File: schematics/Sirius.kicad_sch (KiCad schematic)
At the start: 13 parts, among them J1 DE9_Plug, U1 W65C02SxP, U10 MAX232, U2 W65C51NxP, U3 2764, U4 74LS138, U5 74LS138, X1 TFT680, X2 TFT680

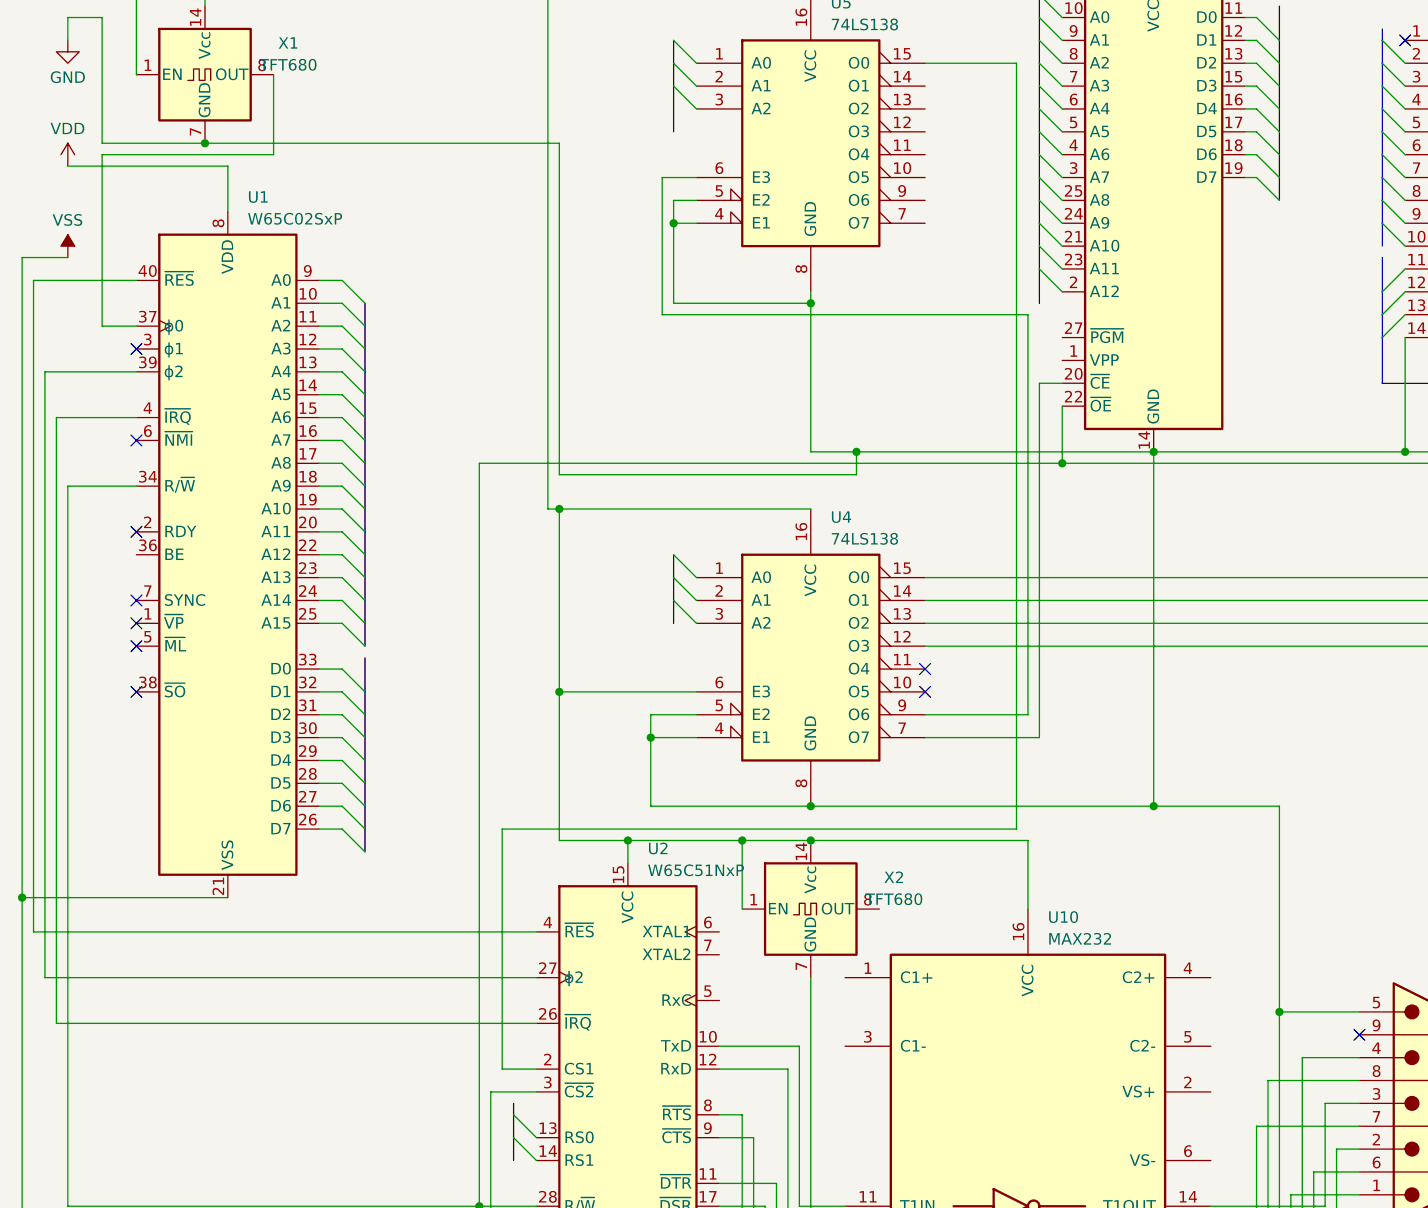
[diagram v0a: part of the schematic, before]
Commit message: Added some more signal handling and caps for rs232 infterface's max232 level shifter.
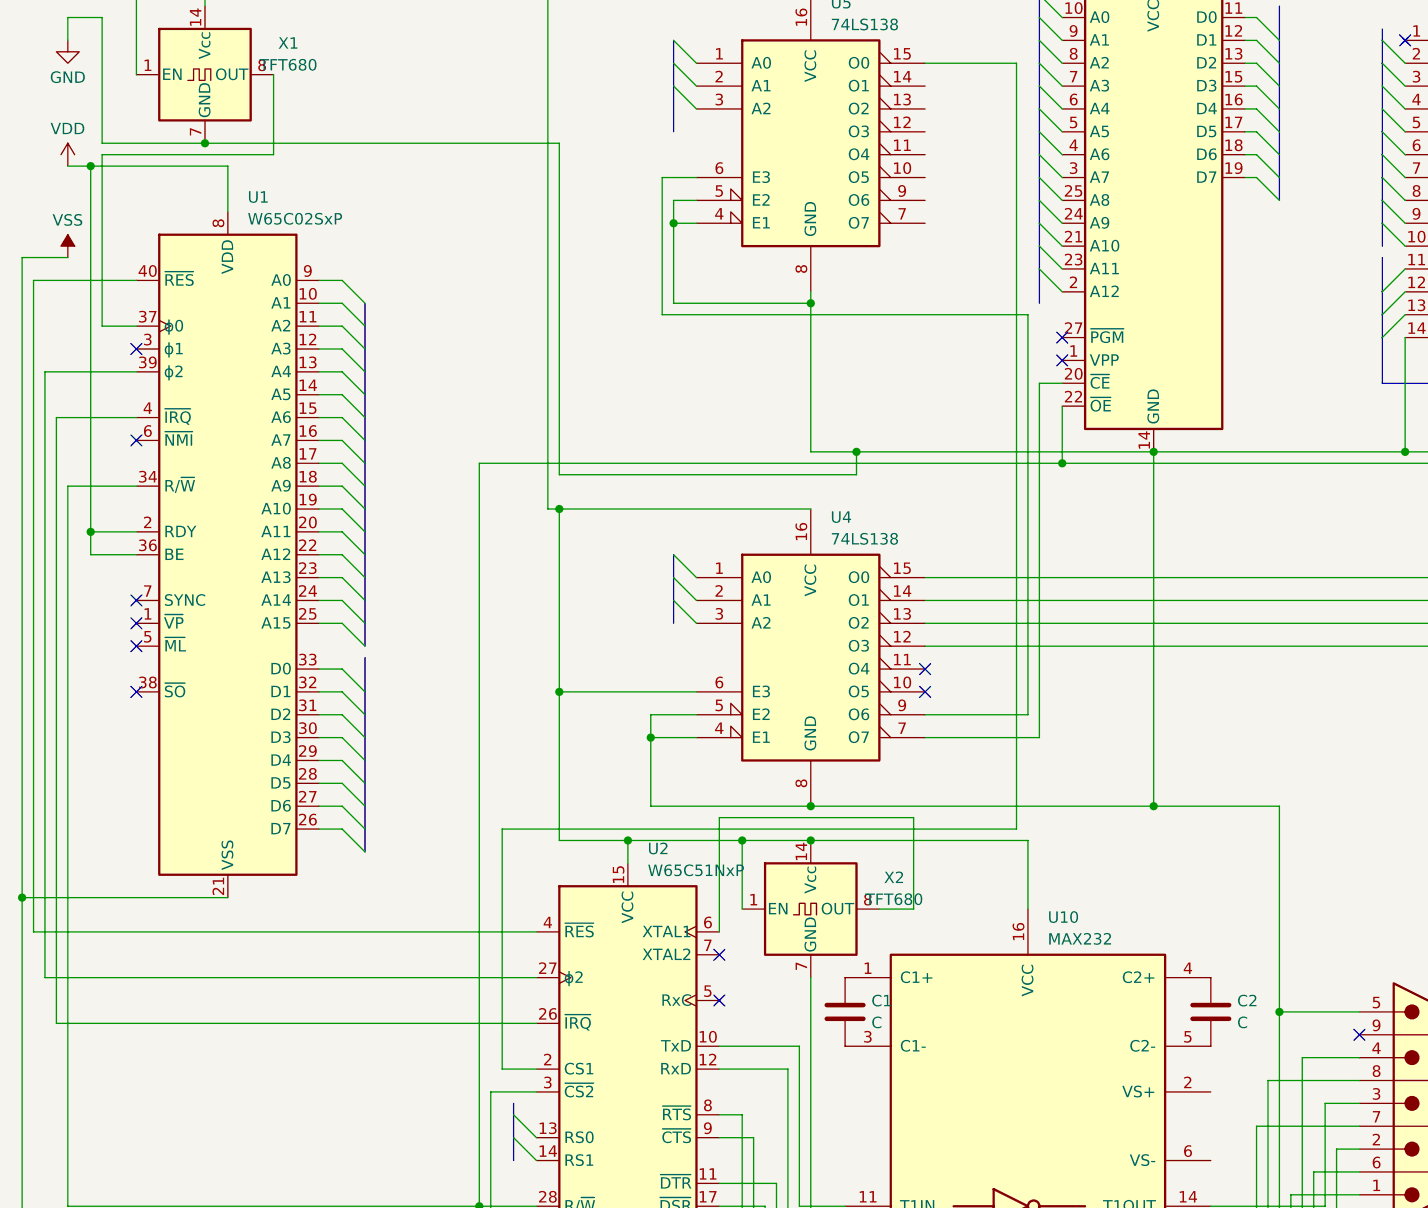
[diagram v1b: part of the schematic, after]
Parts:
- added C1, C2: C, symbol Device:C
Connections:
- net VDD: now also U1.2 (RDY), U1.36 (BE)
- net at U10.1 (C1+): now also C1.1
- net at U10.3 (C1-): now also C1.2
- net at U10.4 (C2+): now also C2.1
- net at U10.5 (C2-): now also C2.2
- net at X2.8 (OUT): now also U2.6 (XTAL1)
- no-connect marks 18 -> 21
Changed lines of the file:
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@@
   (junction (at 80.01 115.57) (diameter 0) (color 0 0 0 0)
   )
+  (junction (at 20.32 81.28) (diameter 0) (color 0 0 0 0)
+  )
   (junction (at 213.36 73.66) (diameter 0) (color 0 0 0 0)
   )
@@
   )
   (junction (at 138.43 72.39) (diameter 0) (color 0 0 0 0)
+  )
+  (junction (at 20.32 40.64) (diameter 0) (color 0 0 0 0)
   )
   (junction (at 191.77 72.39) (diameter 0) (color 0 0 0 0)
@@
   (no_connect (at 217.17 26.67))
   (no_connect (at 25.4 60.96))
+  (no_connect (at 128.27 59.69))
   (no_connect (at 113.03 99.06))
   (no_connect (at 161.29 137.16))
@@
   (no_connect (at 25.4 88.9))
   (no_connect (at 25.4 99.06))
-  (no_connect (at 25.4 81.28))
+  (no_connect (at 90.17 128.27))
   (no_connect (at 191.77 26.67))
+  (no_connect (at 128.27 62.23))
+  (no_connect (at 90.17 133.35))
   (no_connect (at 113.03 96.52))
   (no_connect (at 25.4 71.12))
@@
     (stroke (width 0) (type default))
   )
+  (wire (pts (xy 25.4 83.82) (xy 20.32 83.82))
+    (stroke (width 0) (type default))
+  )
   (bus (pts (xy 265.43 36.83) (xy 265.43 39.37))
     (stroke (width 0) (type default))
@@
     (stroke (width 0) (type default))
   )
+  (wire (pts (xy 20.32 81.28) (xy 20.32 40.64))
+    (stroke (width 0) (type default))
+  )
   (wire (pts (xy 148.59 24.13) (xy 149.86 24.13))
     (stroke (width 0) (type default))
@@
     (stroke (width 0) (type default))
   )
-  (wire (pts (xy 35.56 40.64) (xy 17.78 40.64))
+  (wire (pts (xy 35.56 40.64) (xy 20.32 40.64))
     (stroke (width 0) (type default))
   )
@@
     (stroke (width 0) (type default))
   )
+  (wire (pts (xy 90.17 125.73) (xy 90.17 113.03))
+    (stroke (width 0) (type default))
+  )
   (wire (pts (xy 21.59 58.42) (xy 25.4 58.42))
     (stroke (width 0) (type default))
@@
     (stroke (width 0) (type default))
   )
+  (wire (pts (xy 107.95 123.19) (xy 111.76 123.19))
+    (stroke (width 0) (type default))
+  )
   (bus (pts (xy 237.49 62.23) (xy 237.49 63.5))
     (stroke (width 0) (type default))
@@
     (stroke (width 0) (type default))
   )
+  (wire (pts (xy 20.32 83.82) (xy 20.32 81.28))
+    (stroke (width 0) (type default))
+  )
   (wire (pts (xy 265.43 15.24) (xy 237.49 15.24))
     (stroke (width 0) (type default))
@@
     (stroke (width 0) (type default))
   )
+  (wire (pts (xy 20.32 81.28) (xy 25.4 81.28))
+    (stroke (width 0) (type default))
+  )
   (wire (pts (xy 35.56 121.92) (xy 12.7 121.92))
     (stroke (width 0) (type default))
@@
     (stroke (width 0) (type default))
   )
+  (wire (pts (xy 90.17 113.03) (xy 111.76 113.03))
+    (stroke (width 0) (type default))
+  )
   (bus (pts (xy 242.57 36.83) (xy 242.57 39.37))
     (stroke (width 0) (type default))
@@
     (stroke (width 0) (type default))
   )
+  (wire (pts (xy 111.76 113.03) (xy 111.76 123.19))
+    (stroke (width 0) (type default))
+  )
   (wire (pts (xy 237.49 31.75) (xy 237.49 26.67))
     (stroke (width 0) (type default))
@@
   )
   (wire (pts (xy 92.71 115.57) (xy 100.33 115.57))
+    (stroke (width 0) (type default))
+  )
+  (wire (pts (xy 20.32 40.64) (xy 17.78 40.64))
     (stroke (width 0) (type default))
   )
@@
         (path "/e3ee6ed1-614e-4d59-b188-f08c48d72f8a"
           (reference "U7") (unit 1)
+        )
+      )
+    )
+  )
+  (symbol (lib_id "Device:C") (at 144.78 134.62 0) (unit 1)
+    (in_bom yes) (on_board yes) (dnp no) (fields_autoplaced)
+    (property "Reference" "C2" (at 147.701 133.4079 0)
+      (effects (font (size 1.27 1.27)) (justify left))
+    )
+    (property "Value" "C" (at 147.701 135.8321 0)
+      (effects (font (size 1.27 1.27)) (justify left))
+    )
+    (property "Footprint" "" (at 145.7452 138.43 0)
+      (effects (font (size 1.27 1.27)) hide)
+    )
+    (property "Datasheet" "~" (at 144.78 134.62 0)
+      (effects (font (size 1.27 1.27)) hide)
+    )
+    (pin "1")
+    (pin "2")
+    (instances
+      (project "Sirius"
+        (path "/e3ee6ed1-614e-4d59-b188-f08c48d72f8a"
+          (reference "C2") (unit 1)
         )
       )
@@
         )
       )
+    )
+  )
+  (symbol (lib_id "Device:C") (at 104.14 134.62 0) (unit 1)
+    (in_bom yes) (on_board yes) (dnp no) (fields_autoplaced)
+    (property "Reference" "C1" (at 107.061 133.4079 0)
+      (effects (font (size 1.27 1.27)) (justify left))
+    )
+    (property "Value" "C" (at 107.061 135.8321 0)
+      (effects (font (size 1.27 1.27)) (justify left))
+    )
+    (property "Footprint" "" (at 105.1052 138.43 0)
+      (effects (font (size 1.27 1.27)) hide)
+    )
+    (property "Datasheet" "~" (at 104.14 134.62 0)
+      (effects (font (size 1.27 1.27)) hide)
+    )
+    (pin "1")
+    (pin "2")
+    (instances
+      (project "Sirius"
+        (path "/e3ee6ed1-614e-4d59-b188-f08c48d72f8a"
+          (reference "C1") (unit 1)
+        )
+      )

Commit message: Minor tweaks to signals and PCB layout.
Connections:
- no-connect marks 21 -> 23
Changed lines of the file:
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@@
   (no_connect (at 245.11 26.67))
   (no_connect (at 104.14 161.29))
+  (no_connect (at 144.78 143.51))
   (no_connect (at 144.78 161.29))
   (no_connect (at 25.4 91.44))
@@
   (no_connect (at 191.77 26.67))
   (no_connect (at 128.27 62.23))
+  (no_connect (at 144.78 151.13))
   (no_connect (at 90.17 133.35))
   (no_connect (at 113.03 96.52))

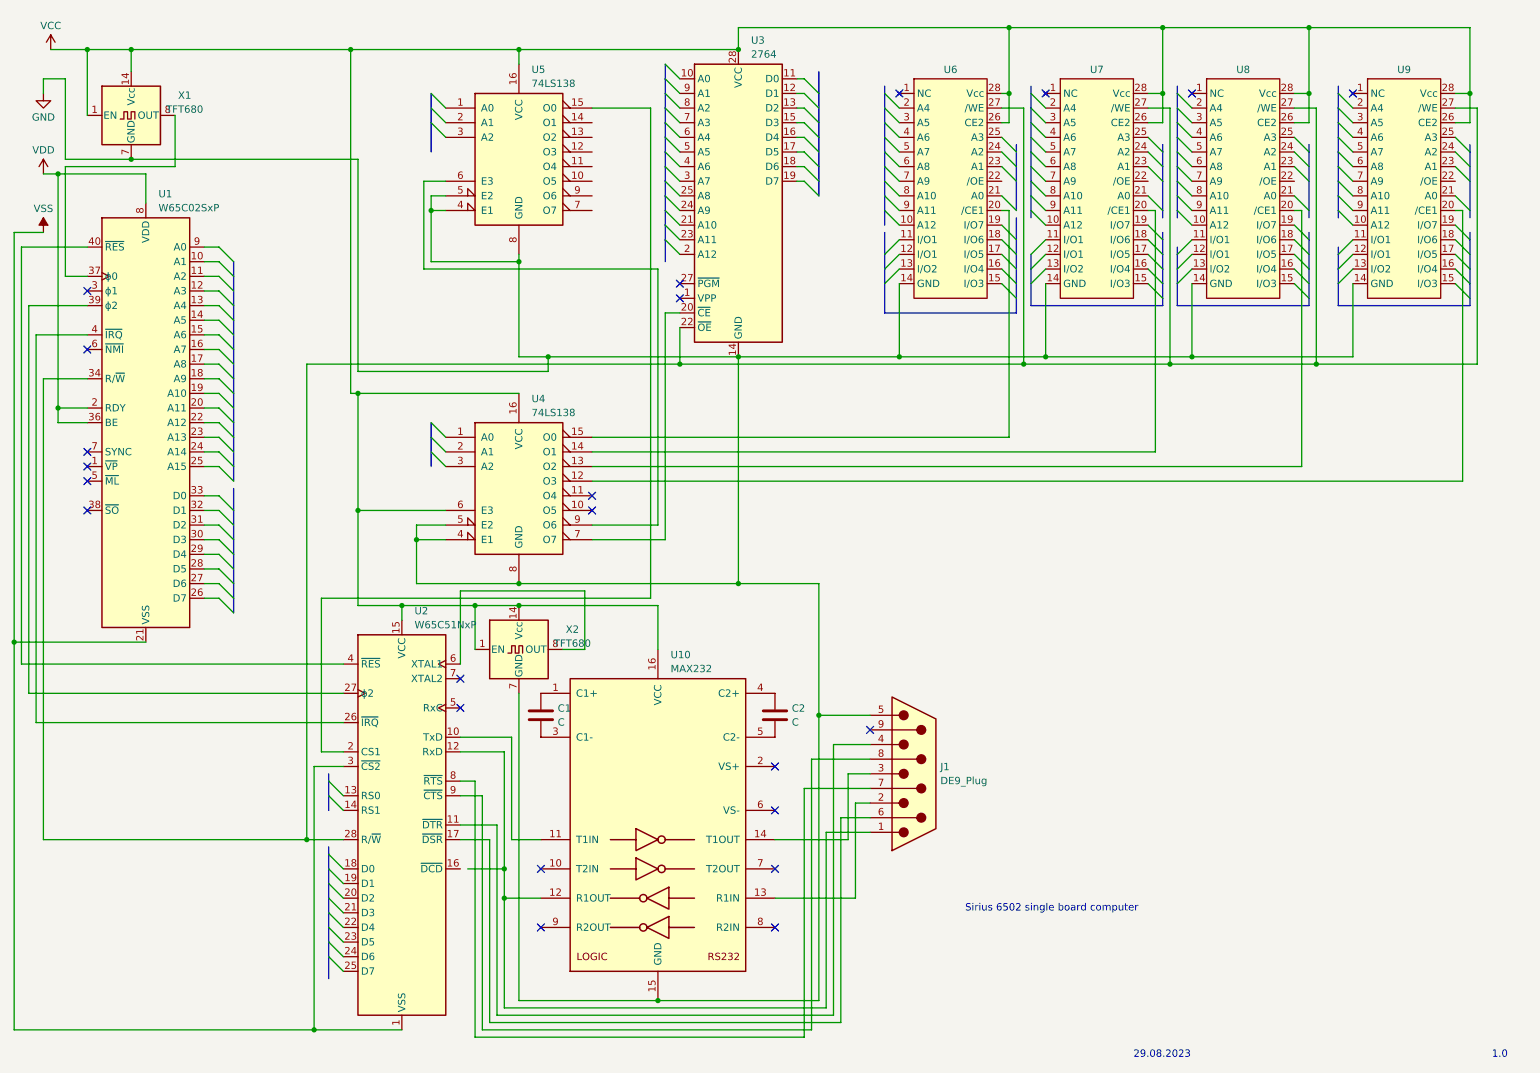
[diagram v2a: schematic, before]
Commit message: Fixed the Bus connetions. Added a forgotten 7404 inverter for R/W signal and did a autorouted board.
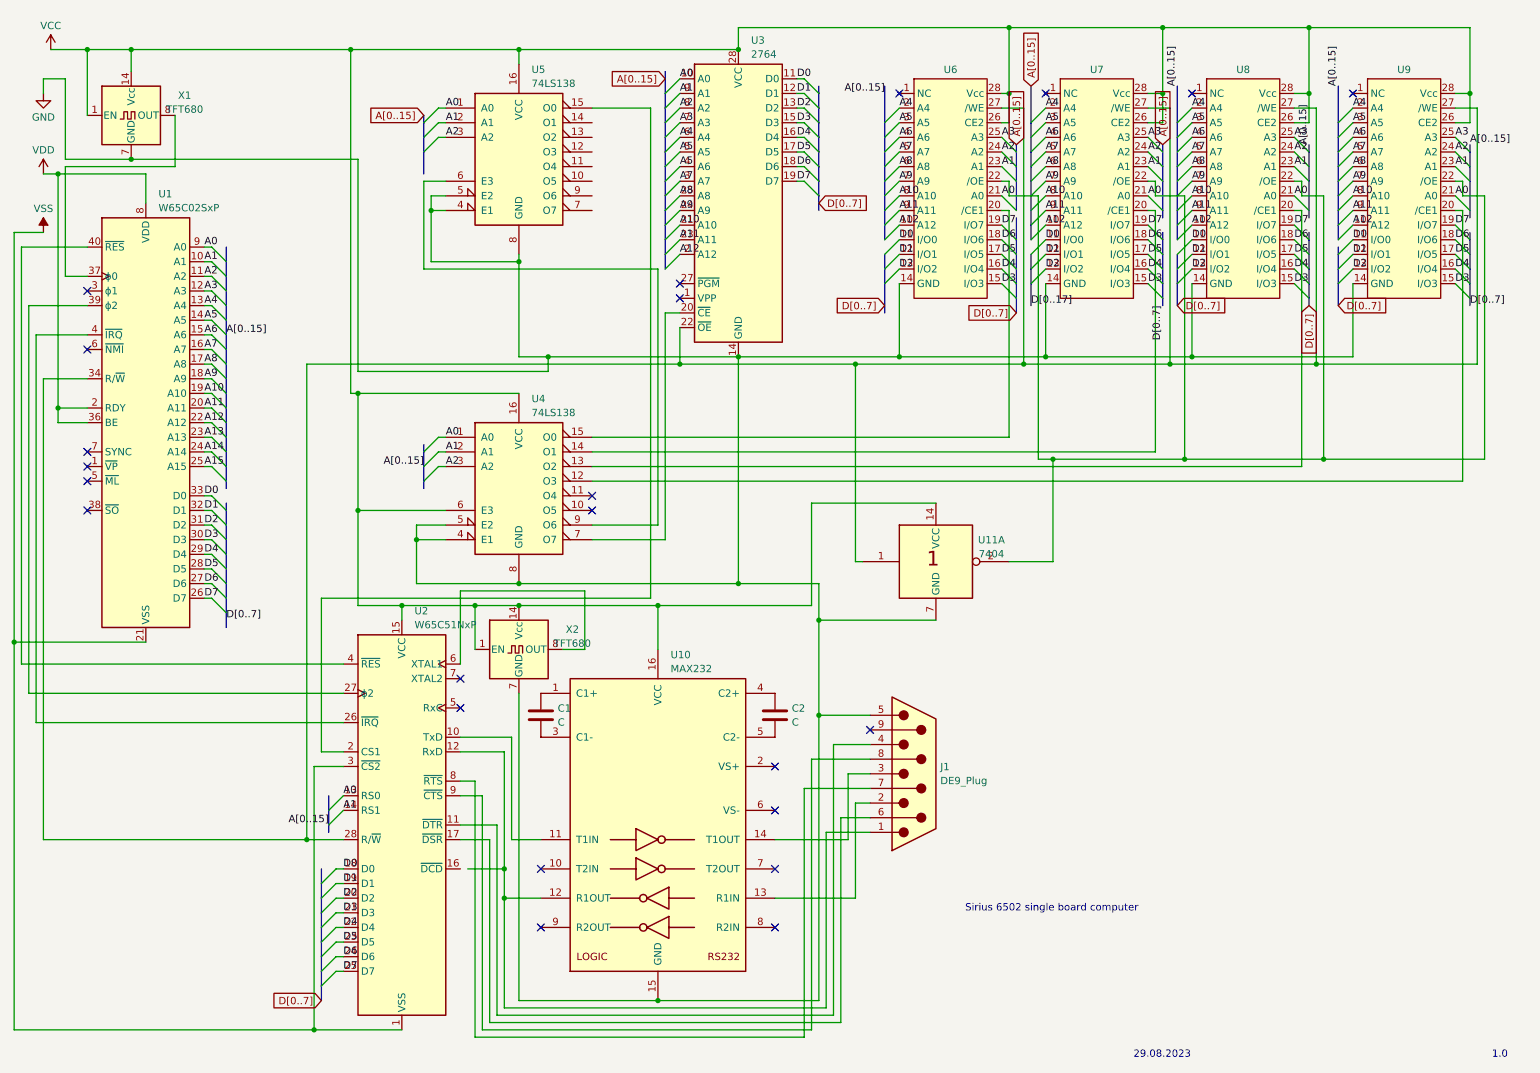
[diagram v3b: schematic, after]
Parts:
- added U11: 7404, Package_DIP:DIP-14_W7.62mm, symbol 74xx_IEEE:7404
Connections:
- net GND: now also U11.7 (GND)
- net VCC: now also U11.14 (VCC)
- net A12: now reaches U9.10 (A12)
- net A12: now also U1.22 (A12), U3.2 (A12), U6.10 (A12), U7.10 (A12), U8.10 (A12)
- net D0: now reaches U9.11 (I/O0)
- net D0: now also U1.33 (D0), U2.18 (D0), U3.11 (D0), U6.11 (I/O0), U7.11 (I/O0), U8.11 (I/O0)
- net D1: now reaches U9.12 (I/O1)
- net D1: now also U1.32 (D1), U2.19 (D1), U3.12 (D1), U6.12 (I/O1), U7.12 (I/O1), U8.12 (I/O1)
- net D2: now reaches U9.13 (I/O2)
- net D2: now also U1.31 (D2), U2.20 (D2), U3.13 (D2), U6.13 (I/O2), U7.13 (I/O2), U8.13 (I/O2)
- net D3: now reaches U9.15 (I/O3)
- net D3: now also U1.30 (D3), U2.21 (D3), U3.15 (D3), U6.15 (I/O3), U7.15 (I/O3), U8.15 (I/O3)
- net D4: now reaches U9.16 (I/O4)
- net D4: now also U1.29 (D4), U2.22 (D4), U3.16 (D4), U6.16 (I/O4), U7.16 (I/O4), U8.16 (I/O4)
- net D5: now reaches U9.17 (I/O5)
- net D5: now also U1.28 (D5), U2.23 (D5), U3.17 (D5), U6.17 (I/O5), U7.17 (I/O5), U8.17 (I/O5)
- net D6: now reaches U9.18 (I/O6)
- net D6: now also U1.27 (D6), U2.24 (D6), U3.18 (D6), U6.18 (I/O6), U7.18 (I/O6), U8.18 (I/O6)
- net D7: now reaches U9.19 (I/O7)
- net D7: now also U1.26 (D7), U2.25 (D7), U3.19 (D7), U6.19 (I/O7), U7.19 (I/O7), U8.19 (I/O7)
- net A4: now reaches U9.2 (A4)
- net A4: now also U1.13 (A4), U3.6 (A4), U6.2 (A4), U7.2 (A4), U8.2 (A4)
- net A0: now reaches U9.21 (A0)
- net A0: now also U1.9 (A0), U2.13 (RS0), U3.10 (A0), U4.1 (A0), U5.1 (A0), U6.21 (A0), U7.21 (A0), U8.21 (A0)
- net at U9.22 (/OE): now also U6.22 (/OE), U7.22 (/OE), U8.22 (/OE), U11.2
- net A1: now reaches U9.23 (A1)
- net A1: now also U1.10 (A1), U2.14 (RS1), U3.9 (A1), U4.2 (A1), U5.2 (A1), U6.23 (A1), U7.23 (A1), U8.23 (A1)
- net A2: now reaches U9.24 (A2)
- net A2: now also U1.11 (A2), U3.8 (A2), U4.3 (A2), U5.3 (A2), U6.24 (A2), U7.24 (A2), U8.24 (A2)
- net A3: now reaches U9.25 (A3)
- net A3: now also U1.12 (A3), U3.7 (A3), U6.25 (A3), U7.25 (A3), U8.25 (A3)
- net at U1.34 (R/~{W}), U2.28 (R/~{W}), U3.22 (~{OE})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: now also U11.1
- net A5: now reaches U9.3 (A5)
- net A5: now also U1.14 (A5), U3.4 (A6), U3.5 (A5), U6.3 (A5), U7.3 (A5), U8.3 (A5)
- net A6: now reaches U9.4 (A6)
- net A6: now also U1.15 (A6), U6.4 (A6), U7.4 (A6), U8.4 (A6)
- net A7: now reaches U9.5 (A7)
- net A7: now also U1.16 (A7), U3.3 (A7), U6.5 (A7), U7.5 (A7), U8.5 (A7)
- net A8: now reaches U9.6 (A8)
- net A8: now also U1.17 (A8), U3.25 (A8), U6.6 (A8), U7.6 (A8), U8.6 (A8)
- net A9: now reaches U9.7 (A9)
- net A9: now also U1.18 (A9), U3.24 (A9), U6.7 (A9), U7.7 (A9), U8.7 (A9)
- net A10: now reaches U9.8 (A10)
- net A10: now also U1.19 (A10), U3.21 (A10), U6.8 (A10), U7.8 (A10), U8.8 (A10)
- net A11: now reaches U9.9 (A11)
- net A11: now also U1.20 (A11), U3.23 (A11), U6.9 (A11), U7.9 (A11), U8.9 (A11)
- net A13: now reaches U1.23 (A13)
- net A14: now reaches U1.24 (A14)
- net A15: now reaches U1.25 (A15)
